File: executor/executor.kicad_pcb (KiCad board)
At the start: 4 copper layers, 58 x 58 mm, 134 parts, among them J1 XT30PW(2+2), J2 gh1.25, 3p, Q1 WNM6006, Q2 WNM6006, Q3 WNM6006, Q4 WNM6006, Q5 WNM6006, Q6 WNM6006, U1 WD1601E, U2 DRV8323SRTAT, U3 GD32F303RETx, U4 TCAN4550RGYRQ1, U5 AS5047P-ATSM, U6 QMA7981, Y1 8M, Y2 40M

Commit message: [New] Fix position for executor
Signed-off-by: Homalozoa <nx.tardis@gmail.com>
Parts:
- removed C22: 47uF, 10% 50V, Capacitor_SMD:CP_Elec_8x6.2
- removed R38: 120R, Resistor_SMD:R_0402_1005Metric
- C1, C11, C13, C14, C15, C18, C19, C2, C20, C21, C3, C4, C5, C7, C8, C9: moved to B.Cu
- C25, C29, Q1, Q2, Q3, Q4, Q5, Q6, R1, R12, R13, R16, R2, R7, R8, R9, TP10, TP7, TP8: moved to F.Cu
- Y1, Y2: footprint Oscillator:Oscillator_SMD_EuroQuartz_XO32-4Pin_3.2x2.5mm -> Oscillator:Oscillator_SMD_ECS_2520MV-xxx-xx-4Pin_2.5x2.0mm
- moved C7 30.1 mm to (97.6, 48.4), turned to 180 degrees
- moved C5 30.1 mm to (97.6, 46.3), turned to 180 degrees
- moved R12 22.1 mm to (94.1, 71.5)
- moved R13 22.0 mm to (83.7, 71.5), turned to 180 degrees
- moved C11 17.4 mm to (99.2, 50.6), turned to 180 degrees
- moved C13 17.4 mm to (99.2, 52.7), turned to 180 degrees
- moved C14 17.4 mm to (99.2, 54.8), turned to 180 degrees
- moved C15 17.4 mm to (99.2, 56.9), turned to 180 degrees
- moved C18 17.4 mm to (99.2, 59.0), turned to 180 degrees
- moved C19 17.4 mm to (99.2, 61.1), turned to 180 degrees
- moved C20 17.4 mm to (99.2, 63.2), turned to 180 degrees
- moved C21 17.4 mm to (99.2, 65.3), turned to 180 degrees
- moved C1 17.4 mm to (99.2, 67.4), turned to 180 degrees
- moved C2 17.4 mm to (99.2, 69.5), turned to 180 degrees
- moved C29 16.2 mm to (81.3, 70.3)
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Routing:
- net +24V: track 201.0 -> 235.6 mm, vias 6 -> 4
- net GNDA: track 161.1 -> 194.1 mm, vias 5 -> 6
- net A: track 85.2 -> 57.1 mm, vias 3 -> 2
- net VGL_C: track 26.1 -> 49.1 mm, vias 3 -> 4
- net VGH_C: track 33.0 -> 51.9 mm
- net ICP: track 39.0 -> 52.4 mm
- net C: track 79.2 -> 68.6 mm
- net VGH_A: track 48.5 -> 38.0 mm, vias 3 -> 2
- net CAN_L: track 61.0 -> 53.3 mm
- net B: track 71.4 -> 64.2 mm
- net VGL_B: track 33.1 -> 38.9 mm, vias 3 -> 4
- net CAN_H: track 55.4 -> 50.8 mm
- net GND: track 302.8 -> 298.6 mm
- net VGH_B: track 43.1 -> 45.6 mm
- net +3V3: track 216.0 -> 217.6 mm
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
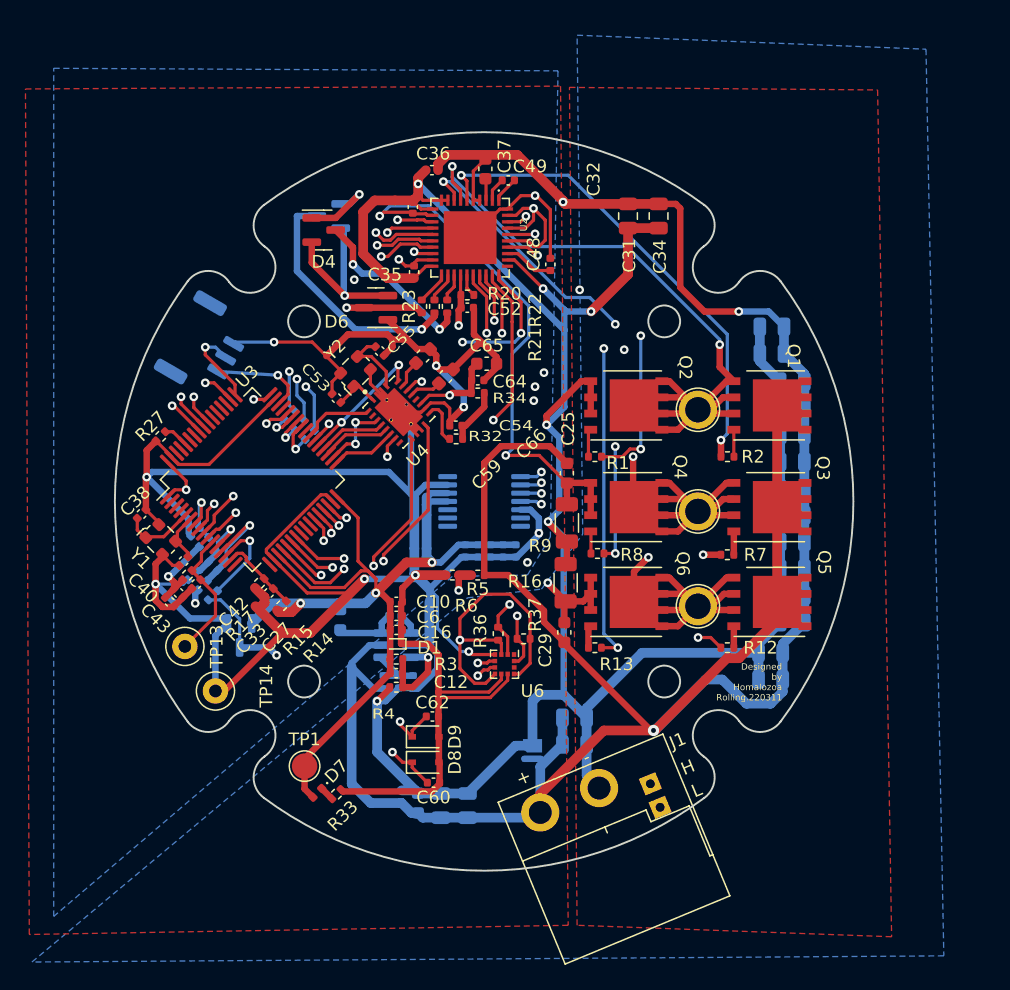
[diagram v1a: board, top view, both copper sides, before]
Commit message: [New] Add 4pin for fast flash
Signed-off-by: Homalozoa <nx.tardis@gmail.com>
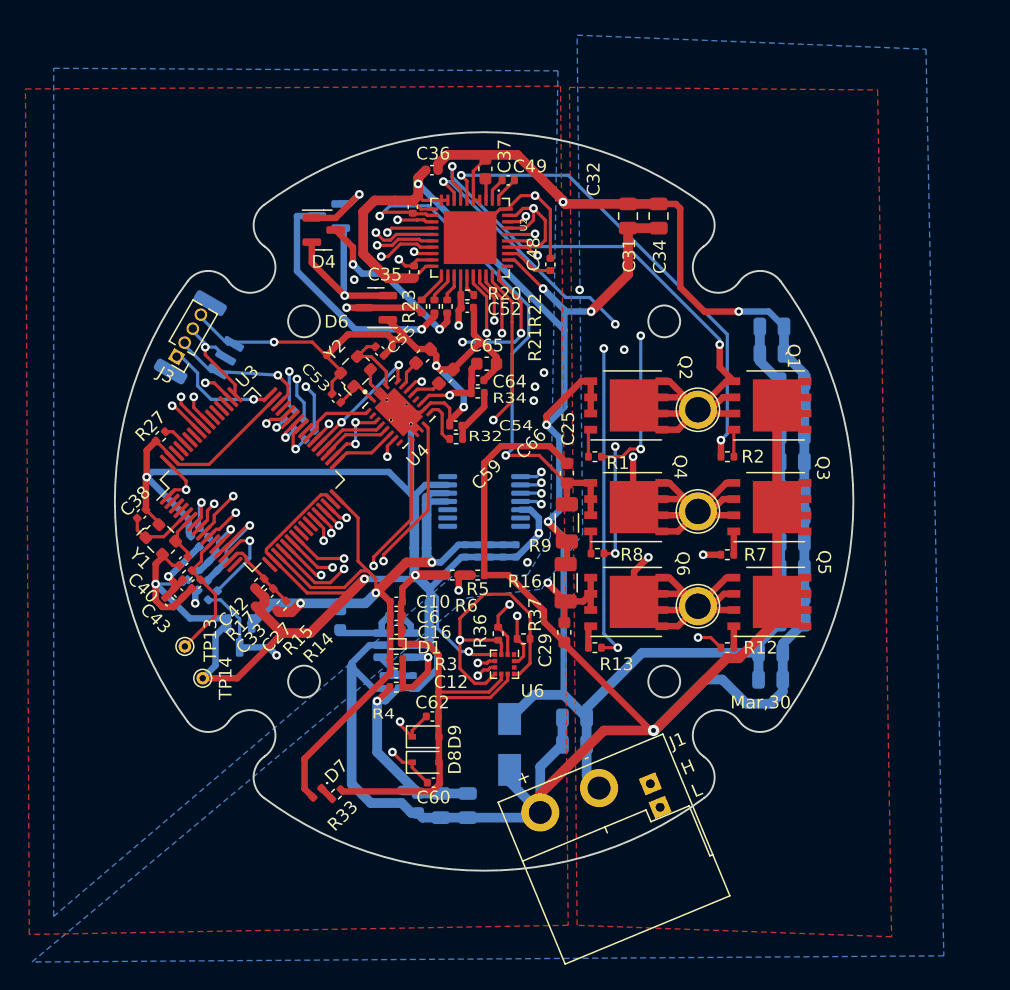
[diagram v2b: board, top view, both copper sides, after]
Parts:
- removed TP1: 3V3, TestPoint:TestPoint_Pad_D2.0mm
- added J3: Conn_01x04, Connector_PinHeader_1.27mm:PinHeader_1x04_P1.27mm_Vertical, F.Cu at (50.9, 48.6)
- D3: value ESD56161D30 -> 30V; footprint Rolling_Custom:DFN2x2-3L -> Diode_SMD:D_SMA
- TP13, TP14: footprint TestPoint:TestPoint_Loop_D1.80mm_Drill1.0mm_Beaded -> TestPoint:TestPoint_THTPad_D1.0mm_Drill0.5mm
- moved D3 1.83 mm to (77.0, 79.1), turned to -90 degrees
- moved TP14 1.41 mm to (52.9, 73.9)
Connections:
- D3 pad 1: +24V -> GNDA
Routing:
- net +3V3: track 217.6 -> 225.8 mm
- net GNDA: track 194.1 -> 186.3 mm
- net SWDIO: track 7.61 -> 11.3 mm
- net GND: track 298.6 -> 302.2 mm
- net +24V: track 235.6 -> 238.6 mm
- net SWCLK: track 6.66 -> 8.53 mm
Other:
- board text added: "Mar,30"
- board text removed: "Designed by Homalozoa Rolling.220311"

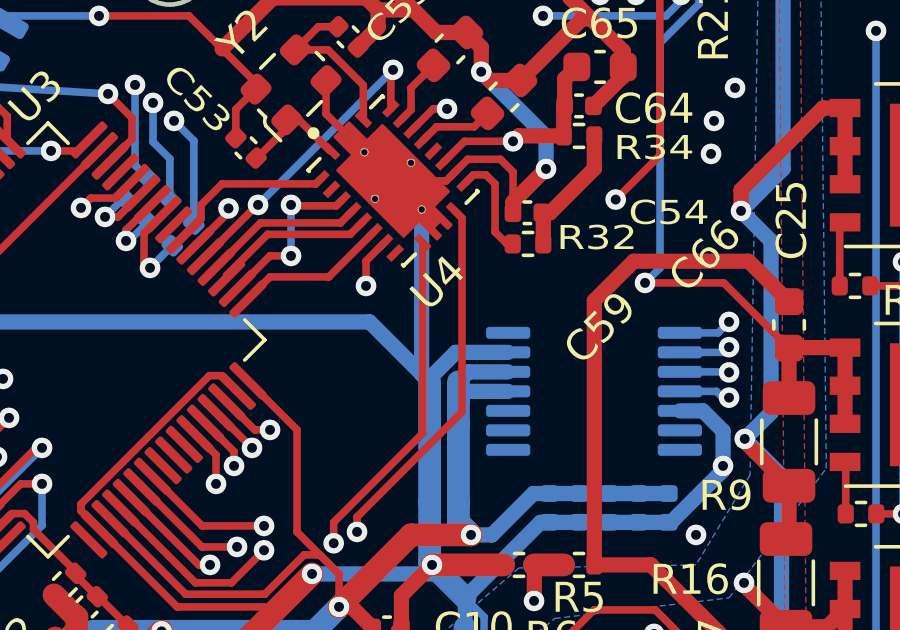
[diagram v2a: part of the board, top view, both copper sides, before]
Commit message: [Modify] Tune length of CAN bus wires
Signed-off-by: Homalozoa X <nx.tardis@gmail.com>
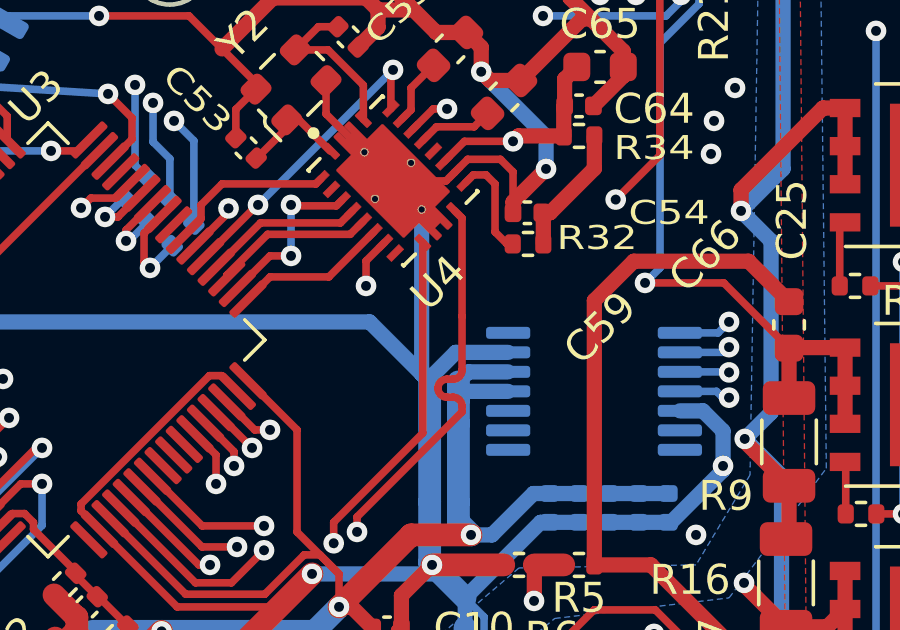
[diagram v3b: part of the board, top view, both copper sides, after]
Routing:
- net CAN_H: track 50.8 -> 52.8 mm
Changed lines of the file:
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@@
   (segment (start 67.3 79.185) (end 67.3 66.485) (width 0.254) (layer "In1.Cu") (net 21))
   (segment (start 68.4 77.285) (end 68.4 77.535) (width 0.254) (layer "F.Cu") (net 22))
+  (segment (start 67.1 64.685) (end 67.1 64.185) (width 0.254) (layer "F.Cu") (net 22))
+  (segment (start 70.6 60.685) (end 70.6 60.495) (width 0.254) (layer "F.Cu") (net 22))
   (segment (start 68.4 77.535) (end 69.35 78.485) (width 0.254) (layer "F.Cu") (net 22))
   (segment (start 69.35 77.9925) (end 70.4575 76.885) (width 0.254) (layer "F.Cu") (net 22))
-  (segment (start 67.1 64.685) (end 67.1 64.185) (width 0.254) (layer "F.Cu") (net 22))
+  (segment (start 70.097663 59.595) (end 70.3 59.595) (width 0.254) (layer "F.Cu") (net 22))
+  (segment (start 70.6 59.295) (end 70.6 57.497454) (width 0.254) (layer "F.Cu") (net 22))
+  (segment (start 70.6 57.497454) (end 70.6 54.224339) (width 0.254) (layer "F.Cu") (net 22))
+  (segment (start 70.3 60.195) (end 70.097663 60.195) (width 0.254) (layer "F.Cu") (net 22))
   (segment (start 67.1 64.185) (end 70.6 60.685) (width 0.254) (layer "F.Cu") (net 22))
-  (segment (start 70.6 60.685) (end 70.6 54.224339) (width 0.254) (layer "F.Cu") (net 22))
   (segment (start 70.6 54.224339) (end 70.35061 53.974949) (width 0.254) (layer "F.Cu") (net 22))
   (segment (start 69.35 78.485) (end 69.35 77.9925) (width 0.254) (layer "F.Cu") (net 22))
   (via (at 67.1 64.685) (size 0.6858) (drill 0.3302) (layers "F.Cu" "B.Cu") (free) (net 22))
   (via (at 68.4 77.285) (size 0.6858) (drill 0.3302) (layers "F.Cu" "B.Cu") (free) (net 22))
+  (arc (start 69.797663 59.895) (mid 69.885531 59.682868) (end 70.097663 59.595) (width 0.254) (layer "F.Cu") (net 22))
+  (arc (start 70.097663 60.195) (mid 69.885531 60.107132) (end 69.797663 59.895) (width 0.254) (layer "F.Cu") (net 22))
+  (arc (start 70.6 60.495) (mid 70.512132 60.282868) (end 70.3 60.195) (width 0.254) (layer "F.Cu") (net 22))
+  (arc (start 70.3 59.595) (mid 70.512132 59.507132) (end 70.6 59.295) (width 0.254) (layer "F.Cu") (net 22))
+  (segment (start 69.48 78.889264) (end 69.367146 79.002117) (width 0.254) (layer "In1.Cu") (net 22))
+  (segment (start 69.79141 79.426381) (end 69.904263 79.313527) (width 0.254) (layer "In1.Cu") (net 22))
+  (segment (start 68.4 77.285) (end 67.68052 76.56552) (width 0.254) (layer "In1.Cu") (net 22))
+  (segment (start 68.4 77.285) (end 68.4 77.385) (width 0.254) (layer "In1.Cu") (net 22))
+  (segment (start 67.68052 66.16552) (end 67.1 65.585) (width 0.254) (layer "In1.Cu") (net 22))
+  (segment (start 67.1 65.585) (end 67.1 64.685) (width 0.254) (layer "In1.Cu") (net 22))
   (segment (start 71.11948 80.10448) (end 85.98733 80.10448) (width 0.254) (layer "In1.Cu") (net 22))
-  (segment (start 68.4 77.285) (end 67.68052 76.56552) (width 0.254) (layer "In1.Cu") (net 22))
-  (segment (start 67.68052 66.16552) (end 67.1 65.585) (width 0.254) (layer "In1.Cu") (net 22))
-  (segment (start 68.4 77.285) (end 68.4 77.385) (width 0.254) (layer "In1.Cu") (net 22))
-  (segment (start 68.4 77.385) (end 71.11948 80.10448) (width 0.254) (layer "In1.Cu") (net 22))
-  (segment (start 67.1 65.585) (end 67.1 64.685) (width 0.254) (layer "In1.Cu") (net 22))
+  (segment (start 69.791411 79.42638) (end 69.79141 79.426381) (width 0.254) (layer "In1.Cu") (net 22))
+  (segment (start 69.479999 78.889265) (end 69.48 78.889264) (width 0.254) (layer "In1.Cu") (net 22))
   (segment (start 85.98733 80.10448) (end 88.054965 82.172115) (width 0.254) (layer "In1.Cu") (net 22))
+  (segment (start 70.328528 79.313528) (end 71.11948 80.10448) (width 0.254) (layer "In1.Cu") (net 22))
+  (segment (start 68.4 77.385) (end 69.48 78.465) (width 0.254) (layer "In1.Cu") (net 22))
   (segment (start 67.68052 76.56552) (end 67.68052 66.16552) (width 0.254) (layer "In1.Cu") (net 22))
+  (segment (start 70.328527 79.313527) (end 70.328528 79.313528) (width 0.254) (layer "In1.Cu") (net 22))
+  (arc (start 69.904263 79.313527) (mid 70.116395 79.225659) (end 70.328527 79.313527) (width 0.254) (layer "In1.Cu") (net 22))
+  (arc (start 69.367146 79.002117) (mid 69.279278 79.214249) (end 69.367146 79.426381) (width 0.254) (layer "In1.Cu") (net 22))
+  (arc (start 69.367146 79.426381) (mid 69.579279 79.514249) (end 69.791411 79.42638) (width 0.254) (layer "In1.Cu") (net 22))
+  (arc (start 69.48 78.465) (mid 69.567868 78.677133) (end 69.479999 78.889265) (width 0.254) (layer "In1.Cu") (net 22))
   (segment (start 71.360589 50.824411) (end 71.003589 51.181411) (width 0.254) (layer "F.Cu") (net 23))
   (segment (start 71.003589 51.181411) (end 69.750035 51.181411) (width 0.254) (layer "F.Cu") (net 23))

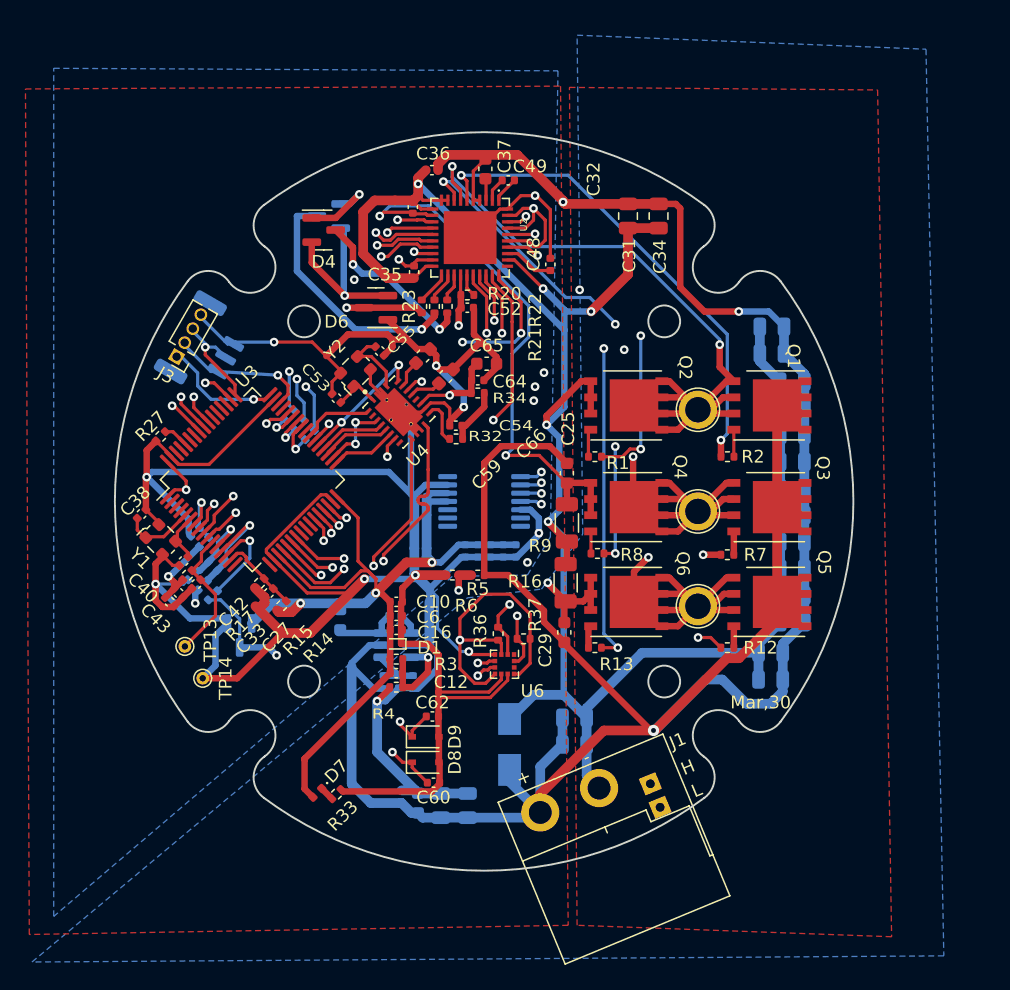
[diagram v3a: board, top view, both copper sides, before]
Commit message: [Fix] Replace dc-dc module to tps & fix xt30-2+2 position
Signed-off-by: Homalozoa <nx.tardis@gmail.com>
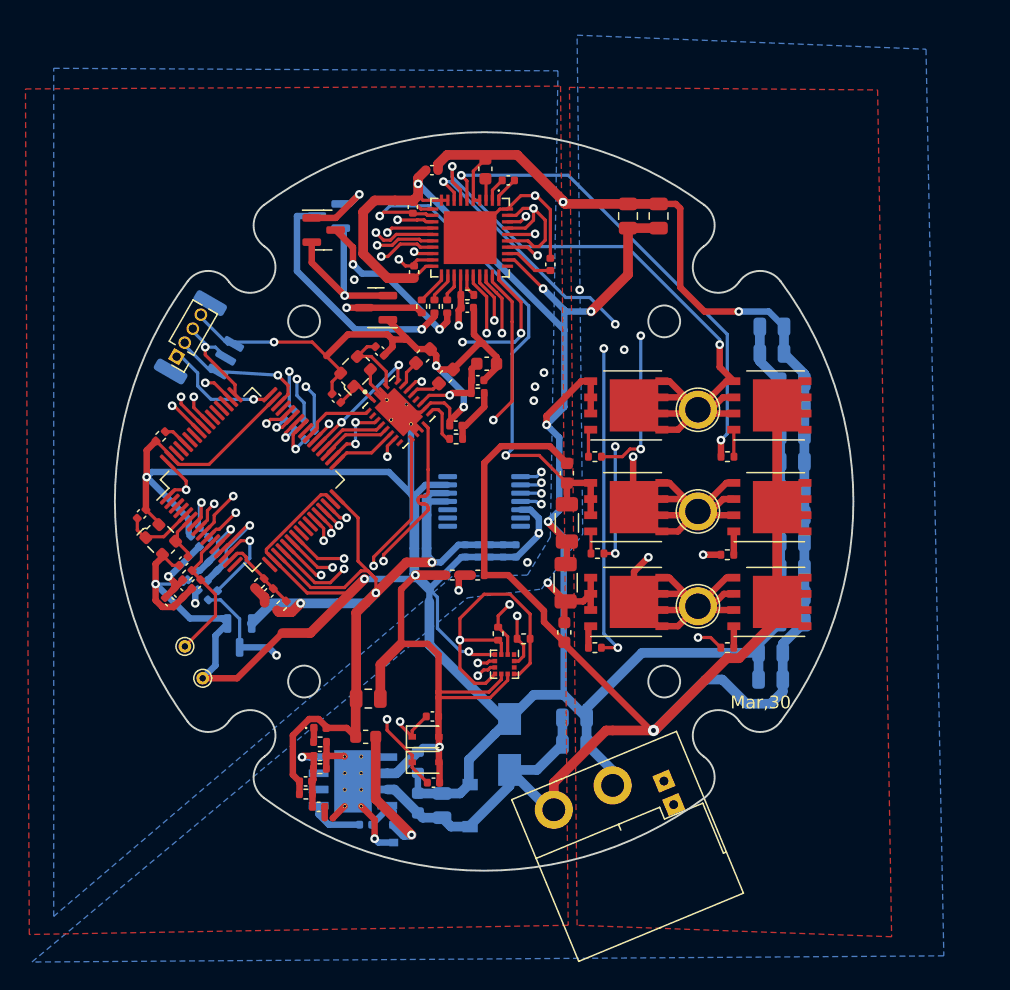
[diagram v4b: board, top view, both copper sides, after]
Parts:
- removed C24, C30: 100nF, 10%, 50V, Capacitor_SMD:C_0402_1005Metric
- removed C26, C28: 4.7uF, 20%, 50V, Capacitor_SMD:C_0805_2012Metric
- removed R11: 100k, 5%, Resistor_SMD:R_0402_1005Metric
- added C22: 100nf 50V, Capacitor_SMD:C_0402_1005Metric, F.Cu at (62.0, 84.0)
- added D10: ESD5Z3V3, Diode_SMD:D_SOD-523, B.Cu at (67.9, 86.1)
- added FB1: 220R, Resistor_SMD:R_0603_1608Metric, B.Cu at (69.8, 80.5)
- C10: value 10uF, 20%, 6.3V -> 10nf 50V; moved to B.Cu
- C12: value 15pF, 5%, 50V -> 100uf 50V; footprint Capacitor_SMD:C_0402_1005Metric -> Capacitor_SMD:C_0805_2012Metric
- C16: value 100nF, 10%, 10V -> 1.5nf 50V
- C23: value 100nF, 10%, 50V -> 150pf 50V; moved to F.Cu
- C6: value 10uF, 20%, 6.3V -> 4.7uF 50V; footprint Capacitor_SMD:C_0402_1005Metric -> Capacitor_SMD:C_0805_2012Metric; moved to B.Cu
- D1: value 5V -> SMF30CA; footprint Diode_SMD:D_SOD-923 -> Diode_SMD:D_SOD-123; moved to B.Cu
- L1: value 10uH -> 15uh; moved to F.Cu
- R10: value 100k, 5% -> 549R; footprint Resistor_SMD:R_0402_1005Metric -> Resistor_SMD:R_0201_0603Metric; moved to F.Cu
- R3: value 150k, 5% -> 10k
- R4: value 47k, 1% -> 5.9k
- U1: value WD1601E -> TPS5430DDAR; footprint Package_TO_SOT_SMD:SOT-23-6 -> Rolling_Custom:TPS5430DDAR
- moved C10 17.7 mm to (65.7, 85.4)
- moved C6 15.3 mm to (71.7, 83.9), turned to 90 degrees
- moved D1 14.0 mm to (73.9, 83.9), turned to -90 degrees
- moved C16 13.9 mm to (61.0, 82.0), turned to 180 degrees
- moved R3 12.8 mm to (61.0, 83.0), turned to 180 degrees
- moved C23 12.5 mm to (62.1, 80.0), turned to 0 degrees
- moved R10 11.5 mm to (62.8, 84.9), turned to 0 degrees
- moved U1 11.2 mm to (64.7, 82.0), turned to 0 degrees
- moved L1 9.41 mm to (65.7, 78.5), turned to 0 degrees
- moved R4 8.77 mm to (62.1, 81.0), turned to 0 degrees
- moved D7 5.10 mm to (62.1, 77.8), turned to 0 degrees
- moved R33 4.30 mm to (62.1, 78.9), turned to 0 degrees
- moved C12 2.97 mm to (65.9, 75.5), turned to 180 degrees
- moved J1 1.09 mm to (84.4, 82.6)
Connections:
- C10 pad 1: +3V3 -> Net-(C10-Pad1)
- C10 pad 2: GND -> Net-(C10-Pad2)
- C12 pad 1: +3V3 -> GND
- C12 pad 2: Net-(C12-Pad2) -> +3V3
- C16 pad 1: +3V3 -> TPS_VSEN
- C16 pad 2: GND -> +3V3
- C23 pad 1: Net-(C23-Pad1) -> TPS_VSEN
- C23 pad 2: Net-(C23-Pad2) -> GND
- C6 pad 1: +3V3 -> +24V
- C6 pad 2: GND -> GNDA
- D1 pad 1: GND -> GNDA
- D1 pad 2: +3V3 -> +24V
- L1 pad 1: Net-(C23-Pad2) -> +3V3
- L1 pad 2: +3V3 -> Net-(C10-Pad2)
- R10 pad 1: +24V -> Net-(C22-Pad2)
- R10 pad 2: Net-(C24-Pad1) -> GND
- R3 pad 1: +3V3 -> TPS_VSEN
- R3 pad 2: Net-(C12-Pad2) -> +3V3
- R4 pad 1: Net-(C12-Pad2) -> TPS_VSEN
- R4 pad 2: GNDA -> GND
- U1 pad 1: Net-(C23-Pad1) -> Net-(C10-Pad1)
- U1 pad 2: GNDA -> unconnected-(U1-Pad2)
- U1 pad 3: Net-(C12-Pad2) -> unconnected-(U1-Pad3)
- U1 pad 4: Net-(C24-Pad1) -> TPS_VSEN
- U1 pad 5: +24V -> unconnected-(U1-Pad5)
- U1 pad 6: Net-(C23-Pad2) -> GND
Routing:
- net +24V: track 238.6 -> 218.8 mm
- net Net-(C10-Pad2): track 0.00 -> 14.3 mm, vias 0 -> 1
- net GND: track 302.2 -> 312.3 mm, vias 12 -> 14
- net Net-(C12-Pad2): track 7.20 -> 0.00 mm, vias 1 -> 0
- net TPS_VSEN: track 0.00 -> 6.28 mm, vias 0 -> 1
- net Net-(C23-Pad2): track 5.01 -> 0.00 mm
- net Net-(C24-Pad1): track 4.31 -> 0.00 mm
- net Net-(C10-Pad1): track 0.00 -> 4.25 mm
- net GNDA: track 186.3 -> 183.0 mm, vias 6 -> 5
- net +3V3: track 225.8 -> 228.8 mm
- net CAN_L: track 53.3 -> 55.8 mm
- net Net-(C23-Pad1): track 1.66 -> 0.00 mm
- net CAN_H: track 52.8 -> 53.8 mm
- net Net-(C22-Pad2): track 0.00 -> 0.90 mm
